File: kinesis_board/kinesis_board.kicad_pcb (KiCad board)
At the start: 2 copper layers, 145 x 100 mm, 42 parts, among them J1 RIGHT_13_TOP, J10 LEFT_13_DOWN, J11 RIGHT_8_TOP, J12 LEFT_8_TOP, J2 RIGHT_13_DOWN, J3 THUMB_RIGHT_SPC_KB600, J4 THUMB_RIGHT_SPC, J5 THUMB_LEFT_BAK, J6 THUMB_LEFT_BAK_KB600, J7 LEFT_1x24, J8 RIGHT_1x24, J9 LEFT_13_TOP

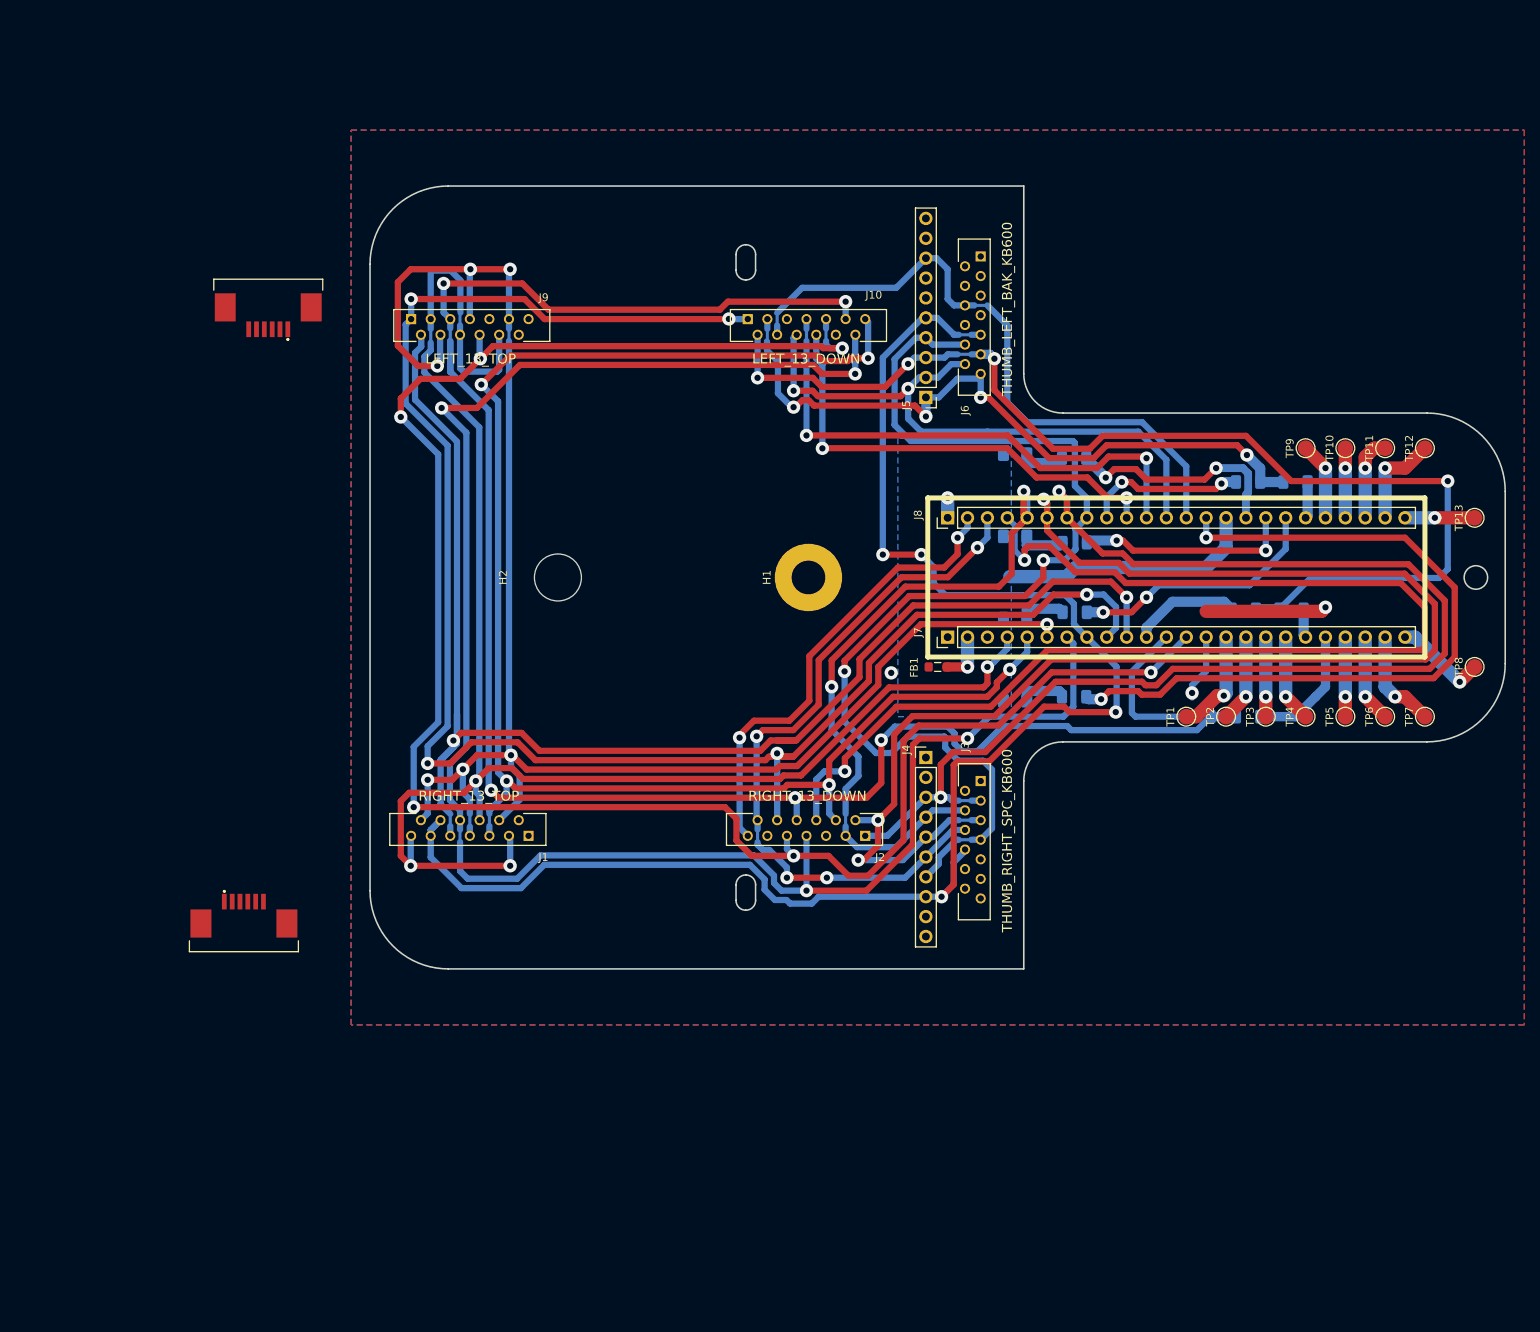
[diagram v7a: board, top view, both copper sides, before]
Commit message: updated pcb to use smalle connector and removed the pin headers from the main pcb
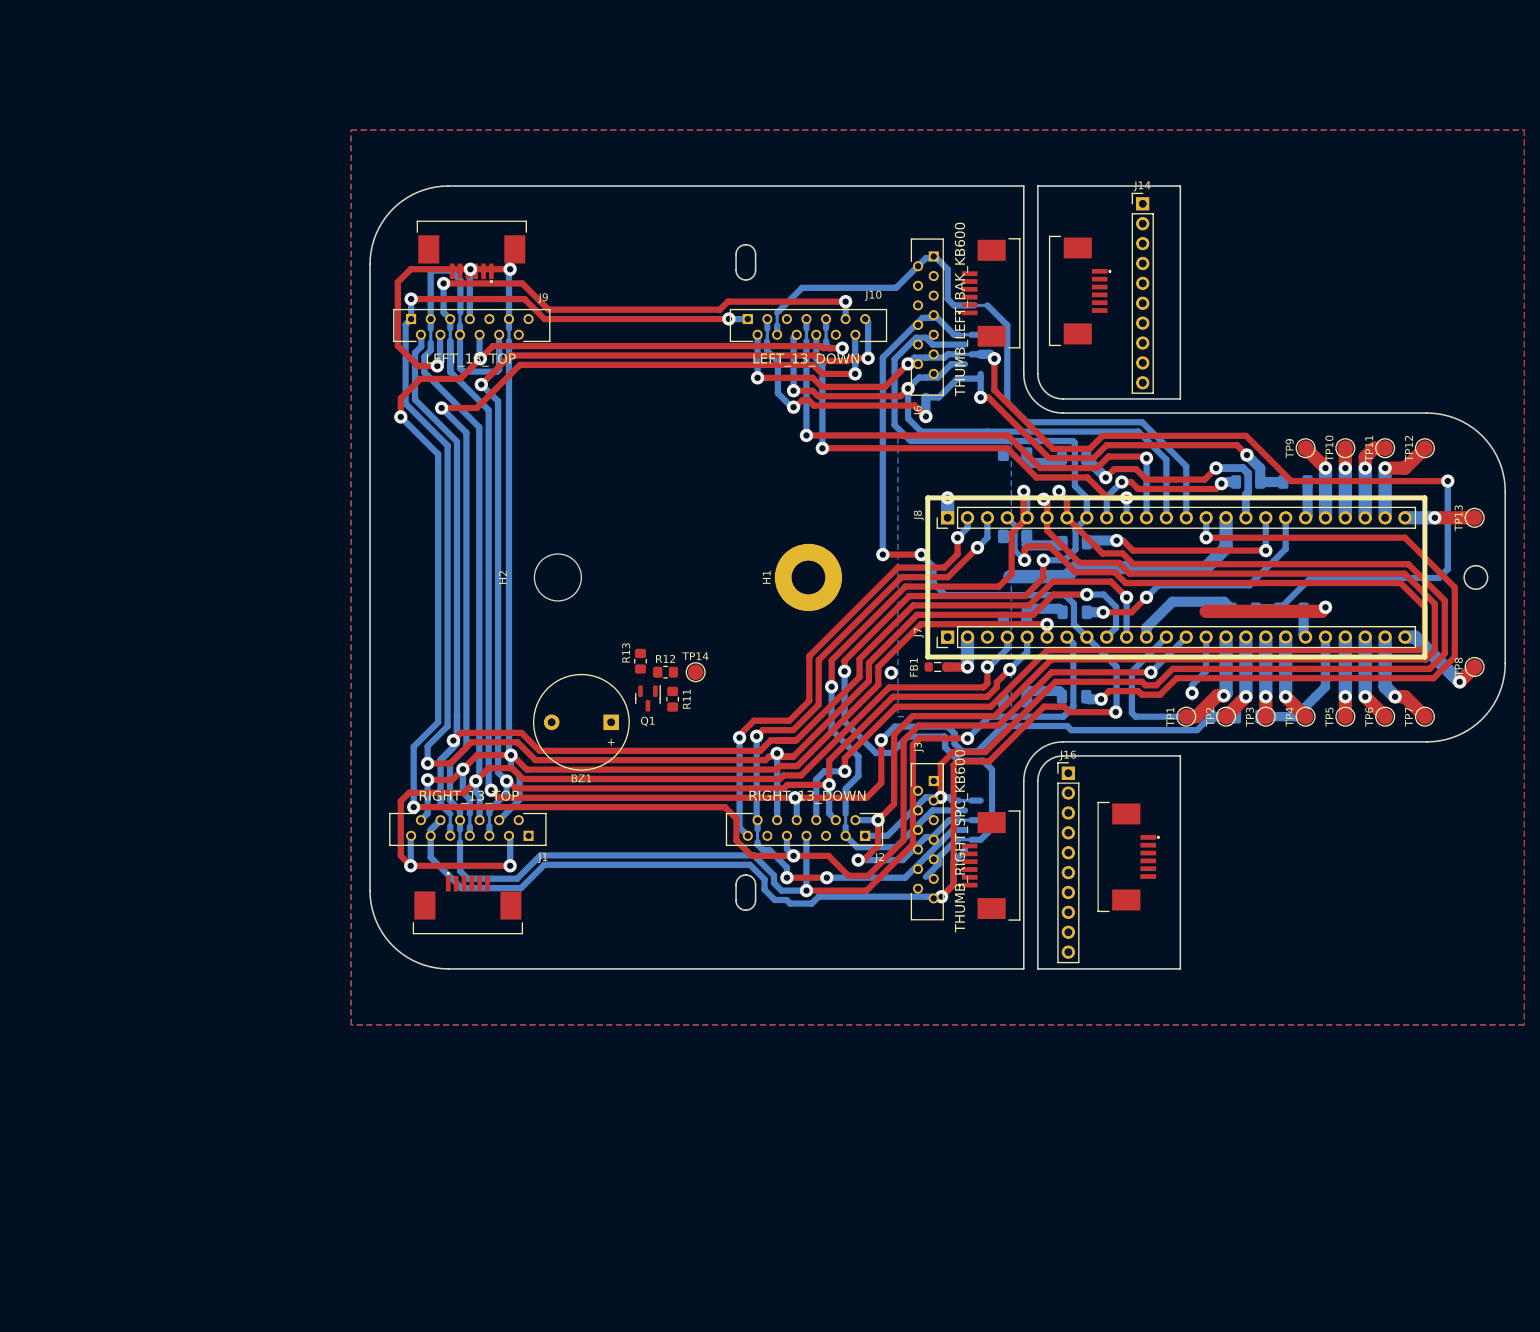
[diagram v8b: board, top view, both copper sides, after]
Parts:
- added BZ1: Buzzer, Buzzer_Beeper:Buzzer_12x9.5RM7.6, F.Cu at (110.9, 109.3)
- added J13: REDUCER_THUMB_RIGHT_6Pins, dodo_conn:84953-6, F.Cu at (170.8, 54.2)
- added J14: REDUCER_THUMB_RIGHT_10Pins, Connector_PinHeader_2.54mm:PinHeader_1x10_P2.54mm_Vertical, F.Cu at (178.8, 43.1)
- added J15: REDUCER_THUMB_LEFT_6Pins, dodo_conn:84953-6, F.Cu at (177.0, 126.5)
- added J16: REDUCER_THUMB_LEFT_10Pins, Connector_PinHeader_2.54mm:PinHeader_1x10_P2.54mm_Vertical, F.Cu at (169.3, 115.8)
- added Q1: 2N7002K, Package_TO_SOT_SMD:SOT-23, F.Cu at (115.6, 106.3)
- added R11: R, Resistor_SMD:R_0805_2012Metric_Pad1.20x1.40mm_HandSolder, F.Cu at (118.8, 106.4)
- added R12: R, Resistor_SMD:R_0805_2012Metric_Pad1.20x1.40mm_HandSolder, F.Cu at (117.9, 102.9)
- added R13: R, Resistor_SMD:R_0805_2012Metric_Pad1.20x1.40mm_HandSolder, F.Cu at (114.7, 101.5)
- added TP14: SOUND, TestPoint:TestPoint_Pad_D2.0mm, F.Cu at (121.7, 102.9)
- J4: value THUMB_RIGHT_SPC -> THUMB_LEFT_6Pins; footprint Connector_PinHeader_2.54mm:PinHeader_1x10_P2.54mm_Vertical -> dodo_conn:84953-6
- J5: value THUMB_LEFT_BAK -> THUMB_RIGHT_6Pins; footprint Connector_PinHeader_2.54mm:PinHeader_1x10_P2.54mm_Vertical -> dodo_conn:84953-6
- moved J5 60.3 mm to (159.2, 127.6), turned to 90 degrees
- moved J4 59.9 mm to (159.2, 54.5), turned to 90 degrees
- moved J12 28.7 mm to (92.6, 132.4)
- moved J11 27.0 mm to (93.1, 49.2)
- moved J3 6.00 mm to (152.1, 116.8)
- moved J6 6.00 mm to (152.1, 49.8)
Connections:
- J4 pad 1: unconnected-(J4-Pin_1-Pad1) -> /ROW_4
- J4 pad 2: unconnected-(J4-Pin_2-Pad2) -> /ROW_2
- J4 pad 3: /ROW_6 -> /ROW_5
- J4 pad 4: /ROW_7 -> /COL_6
- J4 pad 5: /ROW_8 -> /COL_5
- J4 pad 6: /ROW_9 -> /ROW_3
- J4 pad 7: /COL_6 -> GND
- J4 pad 8: /COL_5 -> GND
- J5 pad 1: /ROW_4 -> /ROW_6
- J5 pad 2: /ROW_2 -> /ROW_7
- J5 pad 3: /ROW_5 -> /ROW_8
- J5 pad 4: /COL_6 -> /ROW_9
- J5 pad 5: /COL_5 -> /COL_6
- J5 pad 6: unconnected-(J5-Pin_6-Pad6) -> /COL_5
- J5 pad 7: unconnected-(J5-Pin_7-Pad7) -> GND
- J5 pad 8: /ROW_3 -> GND
- J7 pad 1: unconnected-(J7-Pin_1-Pad1) -> +5V
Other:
- outline, holes or cut-outs redrawn
